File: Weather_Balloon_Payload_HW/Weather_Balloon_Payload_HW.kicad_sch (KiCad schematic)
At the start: 0 parts

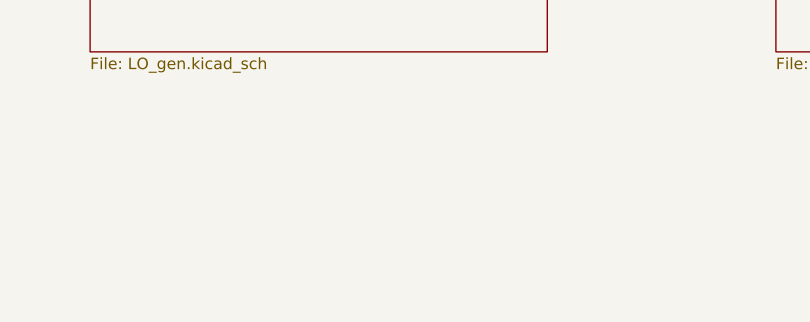
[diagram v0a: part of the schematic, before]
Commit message: Update README, block diagrams, schem. Begin layout
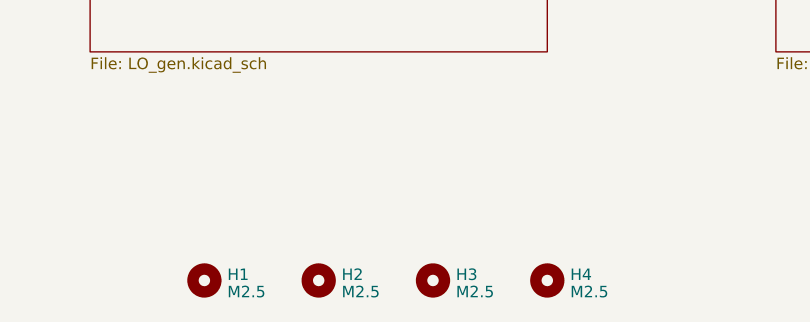
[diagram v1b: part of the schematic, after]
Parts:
- added H1, H2, H3, H4: M2.5, MountingHole:MountingHole_2.7mm_M2.5, symbol Mechanical:MountingHole
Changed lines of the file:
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@@
     (comment 1 "http://acordingley.us")
+  )
+  (symbol (lib_id "Mechanical:MountingHole") (at 139.7 190.5 0) (unit 1)
+    (in_bom yes) (on_board yes) (dnp no) (fields_autoplaced)
+    (property "Reference" "H2" (at 142.24 189.8563 0)
+      (effects (font (size 1.27 1.27)) (justify left))
+    )
+    (property "Value" "M2.5" (at 142.24 191.7773 0)
+      (effects (font (size 1.27 1.27)) (justify left))
+    )
+    (property "Footprint" "MountingHole:MountingHole_2.7mm_M2.5" (at 139.7 190.5 0)
+      (effects (font (size 1.27 1.27)) hide)
+    )
+    (property "Datasheet" "~" (at 139.7 190.5 0)
+      (effects (font (size 1.27 1.27)) hide)
+    )
+    (instances
+      (project "Weather_Balloon_Payload_HW"
+        (path "/5c4ed951-5674-406c-8bab-ae3e3237b79b"
+          (reference "H2") (unit 1)
+        )
+      )
+    )
+  )
+  (symbol (lib_id "Mechanical:MountingHole") (at 165.1 190.5 0) (unit 1)
+    (in_bom yes) (on_board yes) (dnp no) (fields_autoplaced)
+    (property "Reference" "H4" (at 167.64 189.8563 0)
+      (effects (font (size 1.27 1.27)) (justify left))
+    )
+    (property "Value" "M2.5" (at 167.64 191.7773 0)
+      (effects (font (size 1.27 1.27)) (justify left))
+    )
+    (property "Footprint" "MountingHole:MountingHole_2.7mm_M2.5" (at 165.1 190.5 0)
+      (effects (font (size 1.27 1.27)) hide)
+    )
+    (property "Datasheet" "~" (at 165.1 190.5 0)
+      (effects (font (size 1.27 1.27)) hide)
+    )
+    (instances
+      (project "Weather_Balloon_Payload_HW"
+        (path "/5c4ed951-5674-406c-8bab-ae3e3237b79b"
+          (reference "H4") (unit 1)
+        )
+      )
+    )
+  )
+  (symbol (lib_id "Mechanical:MountingHole") (at 152.4 190.5 0) (unit 1)
+    (in_bom yes) (on_board yes) (dnp no) (fields_autoplaced)
+    (property "Reference" "H3" (at 154.94 189.8563 0)
+      (effects (font (size 1.27 1.27)) (justify left))
+    )
+    (property "Value" "M2.5" (at 154.94 191.7773 0)
+      (effects (font (size 1.27 1.27)) (justify left))
+    )
+    (property "Footprint" "MountingHole:MountingHole_2.7mm_M2.5" (at 152.4 190.5 0)
+      (effects (font (size 1.27 1.27)) hide)
+    )
+    (property "Datasheet" "~" (at 152.4 190.5 0)
+      (effects (font (size 1.27 1.27)) hide)
+    )
+    (instances
+      (project "Weather_Balloon_Payload_HW"
+        (path "/5c4ed951-5674-406c-8bab-ae3e3237b79b"
+          (reference "H3") (unit 1)
+        )
+      )
+    )
+  )
+  (symbol (lib_id "Mechanical:MountingHole") (at 127 190.5 0) (unit 1)
+    (in_bom yes) (on_board yes) (dnp no) (fields_autoplaced)
+    (property "Reference" "H1" (at 129.54 189.8563 0)
+      (effects (font (size 1.27 1.27)) (justify left))
+    )
+    (property "Value" "M2.5" (at 129.54 191.7773 0)
+      (effects (font (size 1.27 1.27)) (justify left))
+    )
+    (property "Footprint" "MountingHole:MountingHole_2.7mm_M2.5" (at 127 190.5 0)
+      (effects (font (size 1.27 1.27)) hide)
+    )
+    (property "Datasheet" "~" (at 127 190.5 0)
+      (effects (font (size 1.27 1.27)) hide)
+    )
+    (instances
+      (project "Weather_Balloon_Payload_HW"
+        (path "/5c4ed951-5674-406c-8bab-ae3e3237b79b"
+          (reference "H1") (unit 1)
+        )
+      )
+    )
   )
   (sheet (at 76.2 38.1) (size 50.8 50.8) (fields_autoplaced)
